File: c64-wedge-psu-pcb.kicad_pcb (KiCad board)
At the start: 2 copper layers, 70 x 54 mm, 17 parts, among them U1 LM2576T-5

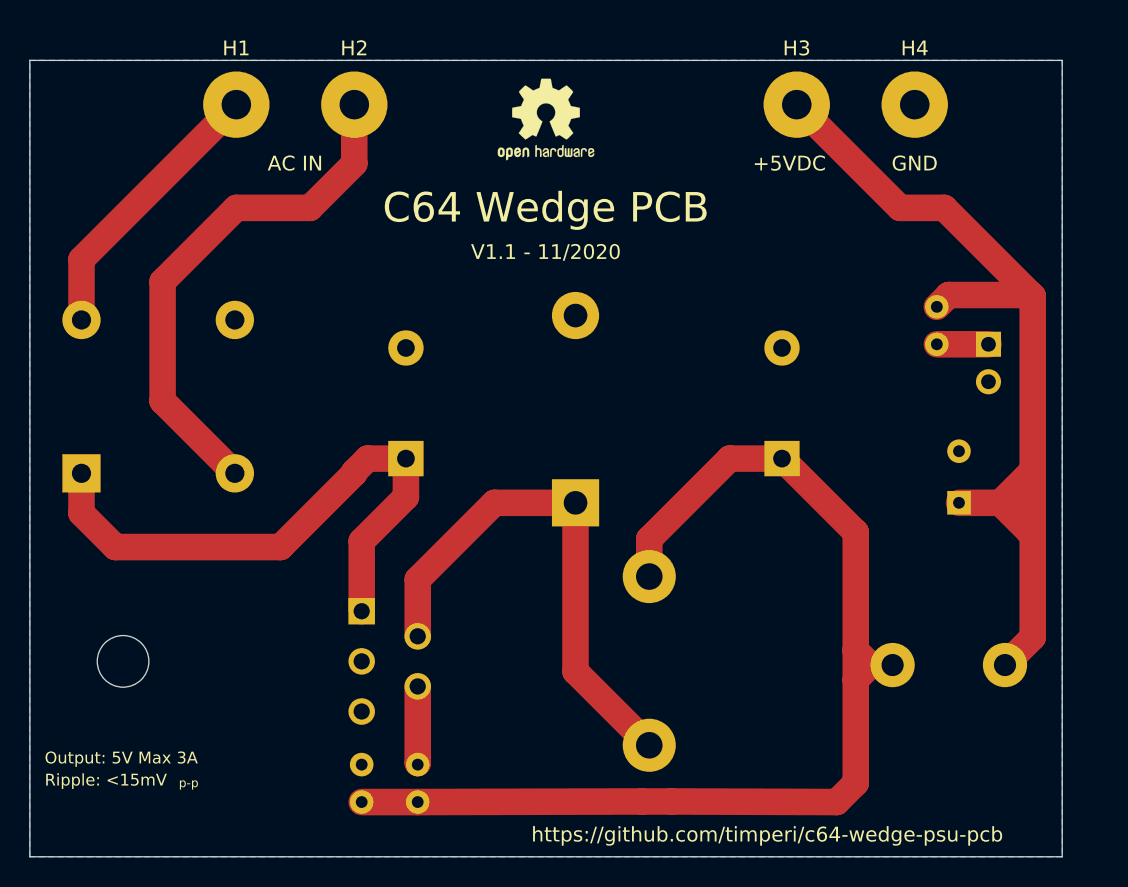
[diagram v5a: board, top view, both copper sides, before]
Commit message: Fix feedback voltage divider (issue #1). Also change resitors to horizontal orientation.
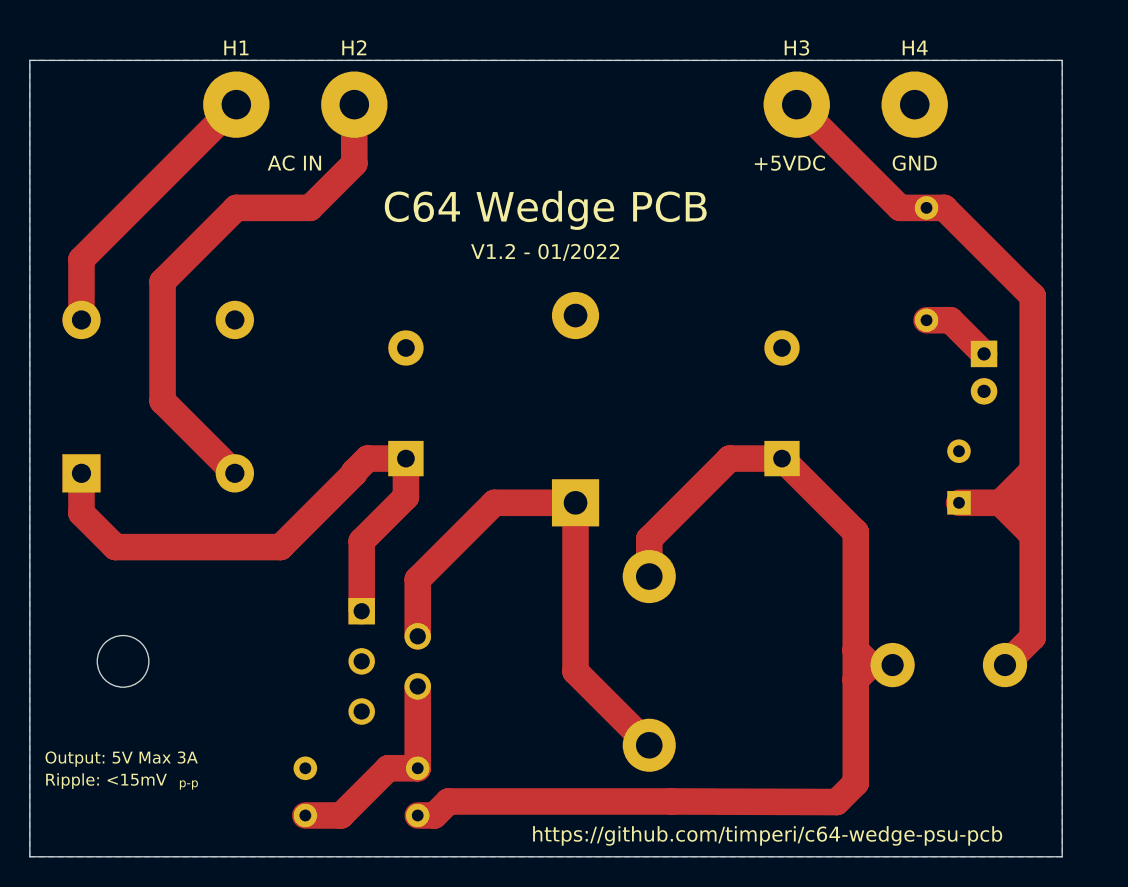
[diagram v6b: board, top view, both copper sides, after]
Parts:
- removed REF**: OSHW-Logo2_7.3x6mm_SilkScreen, Symbol:OSHW-Logo2_7.3x6mm_SilkScreen
- LED1: footprint Connector_PinHeader_2.54mm:PinHeader_1x02_P2.54mm_Vertical -> LED_THT:LED_D3.0mm
- R1, R2, R3: footprint Resistor_THT:R_Axial_DIN0207_L6.3mm_D2.5mm_P2.54mm_Vertical -> Resistor_THT:R_Axial_DIN0207_L6.3mm_D2.5mm_P7.62mm_Horizontal
- moved R2 6.75 mm to (150.8, 70.0)
- moved R3 3.81 mm to (116.3, 108.0), turned to 180 degrees
- moved R1 3.45 mm to (116.3, 111.2), turned to 180 degrees
- moved LED1 0.72 mm to (154.7, 79.9), turned to 270 degrees
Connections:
- R1 pad 1: Net-(R1-Pad1) -> Net-(C2-Pad1)
- R1 pad 2: Net-(C2-Pad1) -> Net-(R1-Pad2)
- R3 pad 1: /GND -> Net-(R1-Pad2)
- R3 pad 2: Net-(C2-Pad1) -> /GND
- U1 pad 4: Net-(R1-Pad1) -> Net-(R1-Pad2)
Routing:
- net Net-(R1-Pad2): track 0.00 -> 14.5 mm
- net /+5VDC: track 64.5 -> 57.8 mm
- net Net-(R1-Pad1): track 5.19 -> 0.00 mm
- net Net-(C2-Pad1): track 76.2 -> 72.8 mm
- net Net-(LED1-Pad1): track 3.50 -> 4.84 mm
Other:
- board text added: "V1.2 - 01/2022"
- board text removed: "V1.1 - 11/2020"

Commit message: Adjust feedback voltage divider resitor values. Reposition led resistor, there is no room in previous position. Minor layout changes.
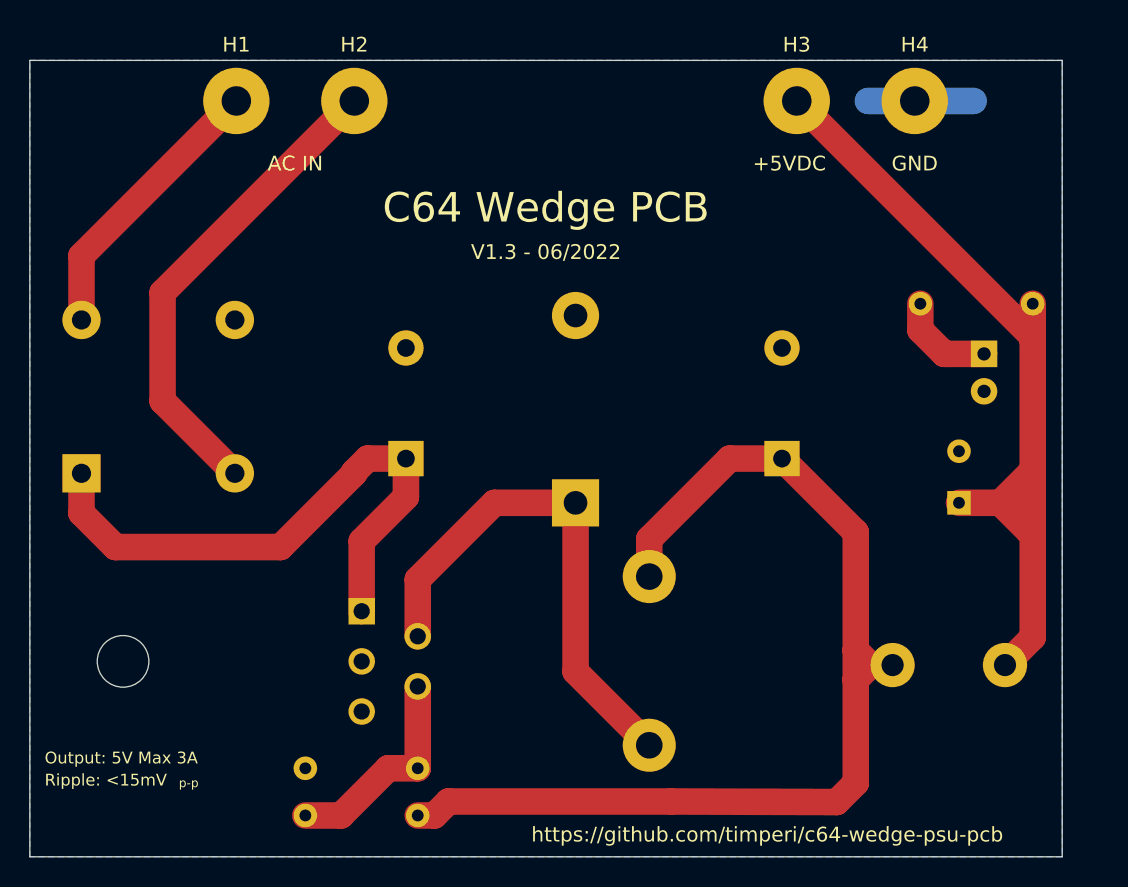
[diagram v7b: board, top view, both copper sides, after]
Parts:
- moved R2 9.70 mm to (158.0, 76.5), turned to 180 degrees
- moved H1 0.25 mm to (104.0, 62.8)
- moved H2 0.25 mm to (112.0, 62.8)
- moved H3 0.25 mm to (142.0, 62.8)
- moved H4 0.25 mm to (150.0, 62.8)
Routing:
- net /GND: track 0.00 -> 7.18 mm
- net Net-(D1-Pad4): track 35.3 -> 32.7 mm
- net Net-(LED1-Pad1): track 4.84 -> 6.77 mm
- net /+5VDC: track 57.8 -> 58.7 mm
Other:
- board text added: "V1.3 - 06/2022"
- board text removed: "V1.2 - 01/2022"
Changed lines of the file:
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@@
     (descr "LED, diameter 3.0mm, 2 pins")
     (tags "LED diameter 3.0mm 2 pins")
-    (fp_text reference LED1 (at 1.27 2.96 90) (layer B.SilkS)
+    (fp_text reference LED1 (at -0.4 4.2 180) (layer B.SilkS)
       (effects (font (size 1 1) (thickness 0.15)) (justify mirror))
     )
@@
   )
   (module Resistor_THT:R_Axial_DIN0207_L6.3mm_D2.5mm_P7.62mm_Horizontal (layer B.Cu)
-    (at 150.8 70 270)
+    (at 158 76.5 180)
     (descr "Resistor, Axial_DIN0207 series, Axial, Horizontal, pin pitch=7.62mm, 0.25W = 1/4W, length*diameter=6.3*2.5mm^2, http://cdn-reichelt.de/documents/datenblatt/B400/1_4W%23YAG.pdf")
     (tags "Resistor Axial_DIN0207 series Axial Horizontal pin pitch 7.62mm 0.25W = 1/4W length 6.3mm diameter 2.5mm")
-    (fp_text reference R2 (at 3.81 2.37 90) (layer B.SilkS)
-      (effects (font (size 1 1) (thickness 0.15)) (justify mirror))
-    )
-    (fp_text value 200R (at 3.81 -2.37 90) (layer B.Fab)
-      (effects (font (size 1 1) (thickness 0.15)) (justify mirror))
-    )
-    (fp_text user %R (at 3.81 0 90) (layer B.Fab)
+    (fp_text reference R2 (at 3.81 0) (layer B.SilkS)
+      (effects (font (size 1 1) (thickness 0.15)) (justify mirror))
+    )
+    (fp_text value 200R (at 3.81 -2.37) (layer B.Fab)
+      (effects (font (size 1 1) (thickness 0.15)) (justify mirror))
+    )
+    (fp_text user %R (at 3.81 0) (layer B.Fab)
       (effects (font (size 1 1) (thickness 0.15)) (justify mirror))
     )
@@
     (fp_line (start 0.66 -1.25) (end 6.96 -1.25) (layer B.Fab) (width 0.1))
     (fp_line (start 0.66 1.25) (end 0.66 -1.25) (layer B.Fab) (width 0.1))
-    (pad 2 thru_hole oval (at 7.62 0 270) (size 1.6 1.6) (drill 0.8) (layers *.Cu *.Mask)
+    (pad 2 thru_hole oval (at 7.62 0 180) (size 1.6 1.6) (drill 0.8) (layers *.Cu *.Mask)
       (net 8 "Net-(LED1-Pad1)"))
-    (pad 1 thru_hole circle (at 0 0 270) (size 1.6 1.6) (drill 0.8) (layers *.Cu *.Mask)
+    (pad 1 thru_hole circle (at 0 0 180) (size 1.6 1.6) (drill 0.8) (layers *.Cu *.Mask)
       (net 7 /+5VDC))
     (model ${KISYS3DMOD}/Resistor_THT.3dshapes/R_Axial_DIN0207_L6.3mm_D2.5mm_P7.62mm_Horizontal.wrl
@@
     (descr "TO-220-5, Horizontal, RM 1.7mm, Pentawatt, Multiwatt-5, staggered type-2, see http://www.analog.com/media/en/package-pcb-resources/package/pkg_pdf/ltc-legacy-to-220/to-220_5_05-08-1421.pdf?domain=www.linear.com, https://www.diodes.com/assets/Package-Files/TO220-5.pdf")
     (tags "TO-220-5 Horizontal RM 1.7mm Pentawatt Multiwatt-5 staggered type-2")
-    (fp_text reference U1 (at 3.4 20.1 90) (layer B.SilkS)
+    (fp_text reference U1 (at 3.65 5.5 180) (layer B.SilkS)
       (effects (font (size 1 1) (thickness 0.15)) (justify mirror))
     )
@@
       (effects (font (size 1 1) (thickness 0.15)) (justify mirror))
     )
-    (fp_text user %R (at 3.4 20.1 90) (layer B.Fab)
+    (fp_text user %R (at 3.65 5.5) (layer B.Fab)
       (effects (font (size 1 1) (thickness 0.15)) (justify mirror))
     )
@@
   )
   (module Connector_Wire:SolderWirePad_1x01_Drill2mm (layer F.Cu)
-    (at 150 63)
+    (at 150 62.75)
     (descr "Wire solder connection")
     (tags connector)
@@
   )
   (module Connector_Wire:SolderWirePad_1x01_Drill2mm (layer F.Cu)
-    (at 142 63)
+    (at 142 62.75)
     (descr "Wire solder connection")
     (tags connector)
@@
   )
   (module Connector_Wire:SolderWirePad_1x01_Drill2mm (layer F.Cu)
-    (at 112 63)
+    (at 112 62.75)
     (descr "Wire solder connection")
     (tags connector)
@@
   )
   (module Connector_Wire:SolderWirePad_1x01_Drill2mm (layer F.Cu)
-    (at 104 63)
+    (at 104 62.75)
     (descr "Wire solder connection")
     (tags connector)
@@
     (effects (font (size 1 1) (thickness 0.15)))
   )
-  (gr_text "V1.2 - 01/2022" (at 125 73) (layer F.SilkS)
+  (gr_text "V1.3 - 06/2022" (at 125 73) (layer F.SilkS)
     (effects (font (size 1 1) (thickness 0.15)))
   )
@@
   (segment (start 116.3 111.2) (end 117.43137 111.2) (width 1.8) (layer F.Cu) (net 2))
   (segment (start 133.5 110.25) (end 144.71 110.29) (width 1.8) (layer F.Cu) (net 2))
-  (segment (start 93.5 73.5) (end 93.5 77.6) (width 1.8) (layer F.Cu) (net 3) (status 20))
-  (segment (start 104 63) (end 93.5 73.5) (width 1.8) (layer F.Cu) (net 3) (status 10))
+  (segment (start 93.5 73.25) (end 104 62.75) (width 1.8) (layer F.Cu) (net 3))
+  (segment (start 93.5 77.6) (end 93.5 73.25) (width 1.8) (layer F.Cu) (net 3))
   (segment (start 99 83.1) (end 103.9 88) (width 1.8) (layer F.Cu) (net 4) (status 20))
-  (segment (start 99 75) (end 99 83.1) (width 1.8) (layer F.Cu) (net 4))
-  (segment (start 112 63) (end 112 67) (width 1.8) (layer F.Cu) (net 4) (status 10))
-  (segment (start 112 67) (end 109 70) (width 1.8) (layer F.Cu) (net 4))
-  (segment (start 104 70) (end 99 75) (width 1.8) (layer F.Cu) (net 4))
-  (segment (start 109 70) (end 104 70) (width 1.8) (layer F.Cu) (net 4))
+  (segment (start 99 75.75) (end 99 83.1) (width 1.8) (layer F.Cu) (net 4))
+  (segment (start 112 62.75) (end 99 75.75) (width 1.8) (layer F.Cu) (net 4))
   (segment (start 132.5 106.44) (end 132.5 106.5) (width 1.8) (layer F.Cu) (net 5) (status 30))
   (segment (start 116.3 99.05) (end 116.3 95.2) (width 1.8) (layer F.Cu) (net 5) (status 10))
@@
   (segment (start 127 101.44) (end 132 106.44) (width 1.8) (layer F.Cu) (net 5) (status 20))
   (segment (start 127 90) (end 127 101.44) (width 1.8) (layer F.Cu) (net 5) (status 10))
+  (segment (start 150 62.75) (end 154 62.75) (width 1.8) (layer B.Cu) (net 6))
+  (segment (start 150 62.75) (end 146.817398 62.75) (width 1.8) (layer B.Cu) (net 6))
   (segment (start 142 63) (end 143 63) (width 1.8) (layer F.Cu) (net 7) (status 30))
   (segment (start 156.12 101) (end 156.636 101) (width 1.8) (layer F.Cu) (net 7) (status 30))
   (segment (start 156.12 101) (end 158 99.12) (width 1.8) (layer F.Cu) (net 7) (status 10))
-  (segment (start 149 70) (end 142 63) (width 1.8) (layer F.Cu) (net 7) (status 20))
-  (segment (start 152 70) (end 149 70) (width 1.8) (layer F.Cu) (net 7))
-  (segment (start 158 76) (end 152 70) (width 1.8) (layer F.Cu) (net 7))
   (segment (start 155.8 90) (end 157.8 92) (width 1.8) (layer F.Cu) (net 7))
   (segment (start 157.8 92) (end 158 92) (width 1.8) (layer F.Cu) (net 7))
@@
   (segment (start 155.8 90) (end 158 87.8) (width 1.8) (layer F.Cu) (net 7))
   (segment (start 158 92) (end 158 87.75) (width 1.8) (layer F.Cu) (net 7))
-  (segment (start 158 87.75) (end 158 76) (width 1.8) (layer F.Cu) (net 7))
-  (segment (start 157.910001 75.910001) (end 158 76) (width 1.8) (layer F.Cu) (net 7))
-  (segment (start 152.42 77.62) (end 154.7 79.9) (width 1.8) (layer F.Cu) (net 8))
-  (segment (start 150.8 77.62) (end 152.42 77.62) (width 1.8) (layer F.Cu) (net 8))
+  (segment (start 158 87.75) (end 158 79) (width 1.8) (layer F.Cu) (net 7))
+  (segment (start 158 77) (end 158 79) (width 1.8) (layer F.Cu) (net 7))
+  (segment (start 158 76.5) (end 158 77) (width 1.8) (layer F.Cu) (net 7))
+  (segment (start 158 78.75) (end 158 79) (width 1.8) (layer F.Cu) (net 7))
+  (segment (start 142 62.75) (end 158 78.75) (width 1.8) (layer F.Cu) (net 7))
+  (segment (start 150.38 78.28) (end 152 79.9) (width 1.8) (layer F.Cu) (net 8))
+  (segment (start 152 79.9) (end 154.7 79.9) (width 1.8) (layer F.Cu) (net 8))
+  (segment (start 150.38 76.5) (end 150.38 78.28) (width 1.8) (layer F.Cu) (net 8))
   (segment (start 116.3 102.45) (end 116.3 108) (width 1.8) (layer F.Cu) (net 9))
   (segment (start 116.3 108) (end 114.3 108) (width 1.8) (layer F.Cu) (net 9))
@@
       )
     )
+  )
+  (zone (net 0) (net_name "") (layer B.Mask) (hatch edge 0.508)
+    (connect_pads (clearance 0.65))
+    (min_thickness 0.254)
+    (fill yes (arc_segments 32) (thermal_gap 0.508) (thermal_bridge_width 0.508))
+    (polygon
+      (pts
+        (xy 105 106.5) (xy 92.5 106.5) (xy 92.5 95) (xy 105 95)
+      )
+    )

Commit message: Update to 1.4
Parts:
- added C4: 0.1uF, Capacitor_THT:C_Disc_D3.0mm_W1.6mm_P2.50mm, F.Cu at (135.3, 76.3)
- added C5: 0.1uF, Capacitor_THT:C_Disc_D3.0mm_W1.6mm_P2.50mm, F.Cu at (139.7, 92.7)
- added C6: 0.1uF, Capacitor_THT:C_Disc_D3.0mm_W1.6mm_P2.50mm, F.Cu at (157.7, 98.8)
- added D3: SB540, Diode_THT:D_DO-201AD_P12.70mm_Horizontal, F.Cu at (100.3, 88.9)
- added D4: SB540, Diode_THT:D_DO-201AD_P12.70mm_Horizontal, B.Cu at (95.2, 88.9)
- added D5: SB540, Diode_THT:D_DO-201AD_P12.70mm_Horizontal, B.Cu at (115.6, 88.9)
- D1: value 6A -> SB540; footprint Diode_THT:Diode_Bridge_Vishay_KBPC6 -> Diode_THT:D_DO-201AD_P12.70mm_Horizontal; moved to F.Cu
- D2: value 5A -> SB540
- H1, H2, H3, H4: footprint Connector_Wire:SolderWirePad_1x01_Drill2mm -> Connector_Wire:SolderWire-1.5sqmm_1x01_D1.7mm_OD3.9mm
- L1: value 150uH -> 100uH
- L2: value 22uH -> 20uH; footprint Inductor_THT:L_Toroid_Vertical_L16.0mm_W8.0mm_P7.62mm -> c64-wedge-psu-pcb:Bourns-6100-220K-RC
- R1: value 200R -> 1k; moved to F.Cu
- R2: value 200R -> 3.2k; moved to F.Cu
- R3: value 4700R -> 200
- U1: value LM2576T-5 -> LM2576T-ADJ; footprint Package_TO_SOT_THT:TO-220-5_P3.4x3.8mm_StaggerEven_Lead7.13mm_TabDown -> Package_TO_SOT_THT:TO-220-5_P3.4x3.7mm_StaggerEven_Lead3.8mm_Vertical
- moved R3 44.3 mm to (156.8, 90.2), turned to 90 degrees
- moved R2 33.9 mm to (128.3, 92.7)
- moved D2 21.6 mm to (105.4, 88.9)
- moved D1 17.0 mm to (110.5, 88.9), turned to 90 degrees
- moved R1 16.0 mm to (116.8, 95.2), turned to -90 degrees
- moved C1 12.8 mm to (128.3, 87.0)
- moved U1 10.6 mm to (102.0, 99.1), turned to 0 degrees
- moved C3 5.60 mm to (154.9, 95.2), turned to 180 degrees
- moved L2 5.59 mm to (151.9, 105.4)
- moved C2 3.78 mm to (144.8, 87.0)
- moved L1 1.52 mm to (132.1, 108.0)
- moved LED1 1.51 mm to (156.2, 80.0), turned to 90 degrees
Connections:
- C1 pad 1: Net-(C1-Pad1) -> Net-(D1-K)
- D1 pad 1: Net-(C1-Pad1) -> Net-(D1-K)
- D1 pad 2: Net-(D1-Pad2) -> Net-(D1-A)
- D2 pad 1: Net-(D2-Pad1) -> Net-(D1-K)
- D2 pad 2: /GND -> Net-(D2-A)
- H1 pad 1: Net-(D1-Pad2) -> Net-(D2-A)
- H2 pad 1: Net-(D1-Pad4) -> Net-(D1-A)
- L1 pad 1: Net-(D2-Pad1) -> Net-(D5-K)
- LED1 pad 1: Net-(LED1-Pad1) -> Net-(LED1-Pin_1)
- R1 pad 1: Net-(C2-Pad1) -> Net-(U1-FB)
- R1 pad 2: Net-(R1-Pad2) -> /GND
- R2 pad 1: /+5VDC -> Net-(C2-Pad1)
- R2 pad 2: Net-(LED1-Pad1) -> Net-(U1-FB)
- R3 pad 1: Net-(R1-Pad2) -> /+5VDC
- R3 pad 2: /GND -> Net-(LED1-Pin_1)
- U1 pad 1: Net-(C1-Pad1) -> Net-(D1-K)
- U1 pad 2: Net-(D2-Pad1) -> Net-(D5-K)
- U1 pad 4: Net-(R1-Pad2) -> Net-(U1-FB)
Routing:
- net Net-(D1-K): track 0.00 -> 94.4 mm
- net Net-(D5-K): track 0.00 -> 55.0 mm
- net Net-(C1-Pad1): track 39.8 -> 0.00 mm
- net Net-(D2-Pad1): track 35.3 -> 0.00 mm
- net Net-(D1-Pad4): track 32.7 -> 0.00 mm
- net Net-(C2-Pad1): track 72.8 -> 42.8 mm
- net Net-(D2-A): track 0.00 -> 27.1 mm
- net Net-(D1-A): track 0.00 -> 26.8 mm
- net Net-(D1-Pad2): track 19.2 -> 0.00 mm
- net Net-(U1-FB): track 0.00 -> 14.6 mm
- net Net-(R1-Pad2): track 14.5 -> 0.00 mm
- net /GND: track 7.18 -> 0.00 mm
- net Net-(LED1-Pad1): track 6.77 -> 0.00 mm
- net Net-(LED1-Pin_1): track 0.00 -> 2.80 mm
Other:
- net class Default removed
- board text added: "V1.4- 03/2026"
- board text removed: "V1.3 - 06/2022"
